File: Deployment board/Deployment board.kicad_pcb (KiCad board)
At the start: 4 copper layers, 39 x 62 mm, 32 parts, among them J1 Conn_01x04, J2 Conn_01x04, J3 Conn_01x02, J4 Conn_01x02, J5 Conn_01x02, J6 REMOVE BEFORE FLIGHT, J7 Conn_01x02, Q1 IRLR7843, Q2 IRLR7843, Q3 RM40P40LD, Q4 IRLR7843

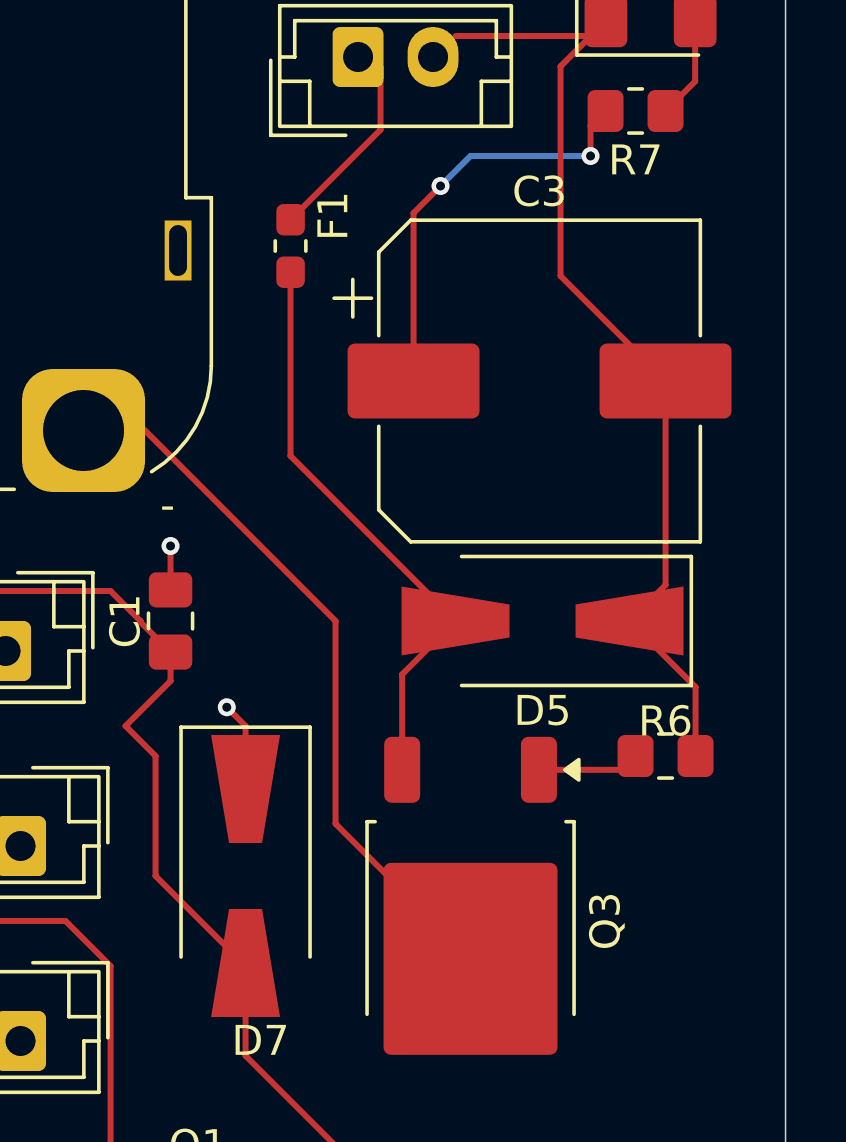
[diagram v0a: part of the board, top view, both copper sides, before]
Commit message: jpush deployment board
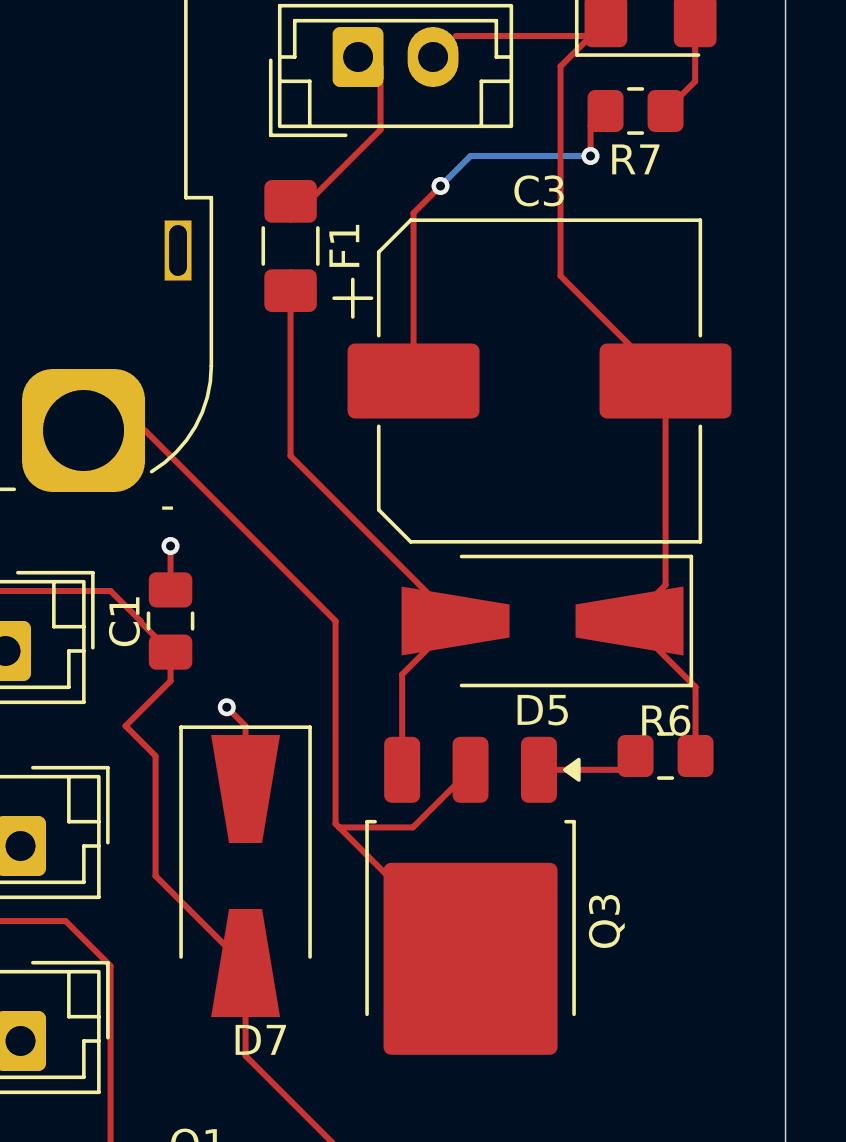
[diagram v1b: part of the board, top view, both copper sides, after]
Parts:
- C1: value 100n -> 77-VJ0805Y104KCAAJ
- C3: value 667-EEH-ZS1E102UP(1000u) -> 667-EEH-ZS1E102UP
- D3, D4, D6, D8: value LED -> 755-SML-S13UTT68
- D5: value TVS -> 652-SMAJ15CA
- D7: value SS54 -> 750-SS54BF-HF
- F1: value Fuse (>15A) -> 652-SF-1206HV15M-2; footprint Fuse:Fuse_0603_1608Metric_Pad1.05x0.95mm_HandSolder -> Fuse:Fuse_1206_3216Metric_Pad1.42x1.75mm_HandSolder
- Q3: value RM40P40LD -> FDD4141; footprint Package_TO_SOT_SMD:TO-252-2 -> Package_TO_SOT_SMD:TO-252-3_TabPin2
- R1, R2, R3: value 1k -> 708-RNAN0805BKE1K00
- R4, R5, R7, R8: value 3.3k -> 667-ERA-6ARB332V
- R6: value 100k -> 594-MCU0805PC1003FP5
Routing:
- net V_D_BAT+: track 18.4 -> 31.6 mm
- net Net-(J6-A): track 24.2 -> 29.3 mm
- net Net-(Q3-G): track 3.41 -> 2.76 mm
